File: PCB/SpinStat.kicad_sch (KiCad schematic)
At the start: 0 parts

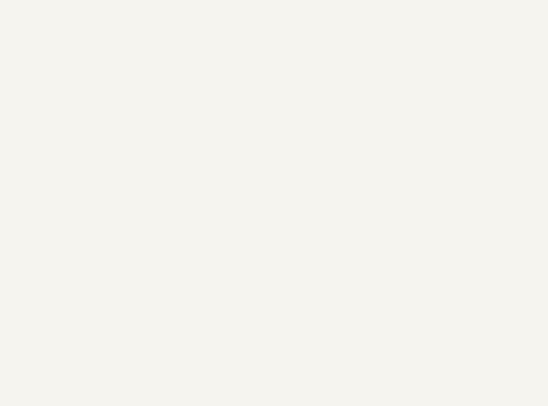
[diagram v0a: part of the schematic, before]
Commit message: added button matrix§
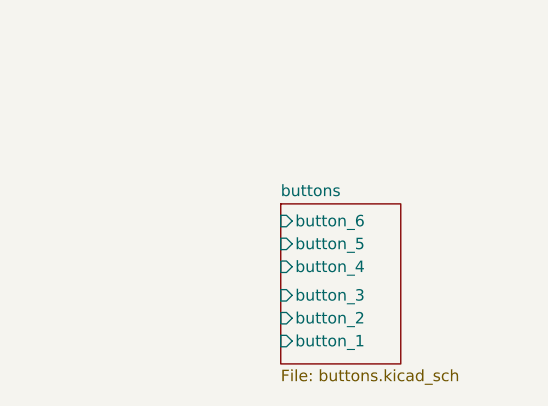
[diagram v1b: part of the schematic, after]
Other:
- added sheet buttons (buttons.kicad_sch)
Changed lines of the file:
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@@
 	(paper "A4")
+	(sheet
+		(at 165.735 76.2)
+		(size 13.335 17.78)
+		(exclude_from_sim no)
+		(in_bom yes)
+		(on_board yes)
+		(dnp no)
+		(fields_autoplaced yes)
+		(stroke
+			(width 0.1524)
+			(type solid)
+		)
+		(fill
+			(color 0 0 0 0.0000)
+		)
+		(property "Sheetname" "buttons"
+			(at 165.735 75.4884 0)
+			(effects
+				(font
+					(size 1.27 1.27)
+				)
+				(justify left bottom)
+			)
+		)
+		(property "Sheetfile" "buttons.kicad_sch"
+			(at 165.735 94.5646 0)
+			(effects
+				(font
+					(size 1.27 1.27)
+				)
+				(justify left top)
+			)
+		)
+		(pin "button_1" input
+			(at 165.735 91.44 180)
+			(effects
+				(font
+					(size 1.27 1.27)
+				)
+				(justify left)
+			)
+		)
+		(pin "button_2" input
+			(at 165.735 88.9 180)
+			(effects
+				(font
+					(size 1.27 1.27)
+				)
+				(justify left)
+			)
+		)
+		(pin "button_3" input
+			(at 165.735 86.36 180)
+			(effects
+				(font
+					(size 1.27 1.27)
+				)
+				(justify left)
+			)
+		)
+		(pin "button_4" input
+			(at 165.735 83.185 180)
+			(effects
+				(font
+					(size 1.27 1.27)
+				)
+				(justify left)
+			)
+		)
+		(pin "button_5" input
+			(at 165.735 80.645 180)
+			(effects
+				(font
+					(size 1.27 1.27)
+				)
+				(justify left)
+			)
+		)
+		(pin "button_6" input
+			(at 165.735 78.105 180)
+			(effects
+				(font
+					(size 1.27 1.27)
+				)
+				(justify left)
+			)
+		)
+		(instances
+			(project "SpinStat"
+				(path "/ffc67360-c592-42dc-bf10-3ceba40203bd"
+					(page "3")
+				)
+			)
+		)
+	)
 	(sheet
 		(at 43.18 29.21)
